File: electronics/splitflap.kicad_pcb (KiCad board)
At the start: 2 copper layers, 96 x 48 mm, 39 parts, among them CON1 MOTOR_PWR, J1 EXP. IN, J2 EXP. OUT, P1 CONN_01X05, P10 CONN_01X04, P2 CONN_01X05, P3 CONN_01X05, P4 CONN_01X05, P6 CONN_01X04, P7 CONN_01X04, P8 CONN_01X04, U1 arduino_uno_shield, U2 MIC5842, U3 74HC165, U4 MIC5842, U5 WS2812B, U6 WS2812B, U7 WS2812B, U8 WS2812B

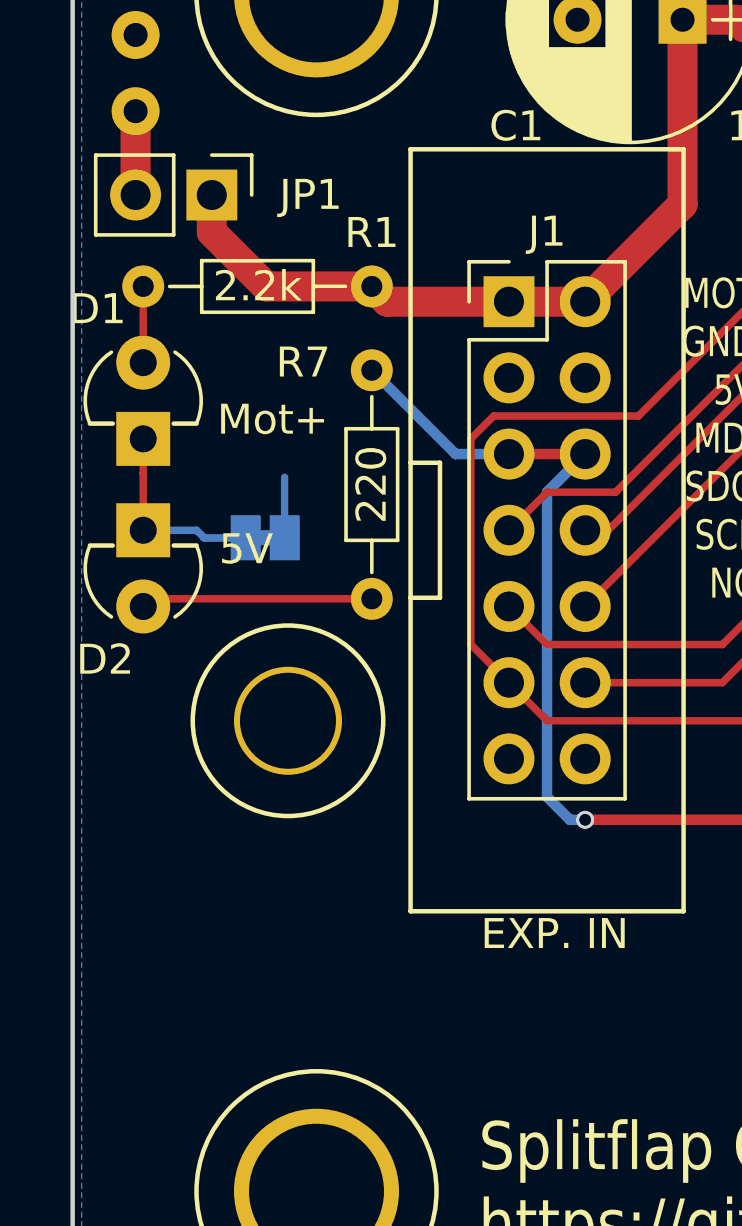
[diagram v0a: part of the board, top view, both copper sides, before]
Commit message: Move power LEDs lower
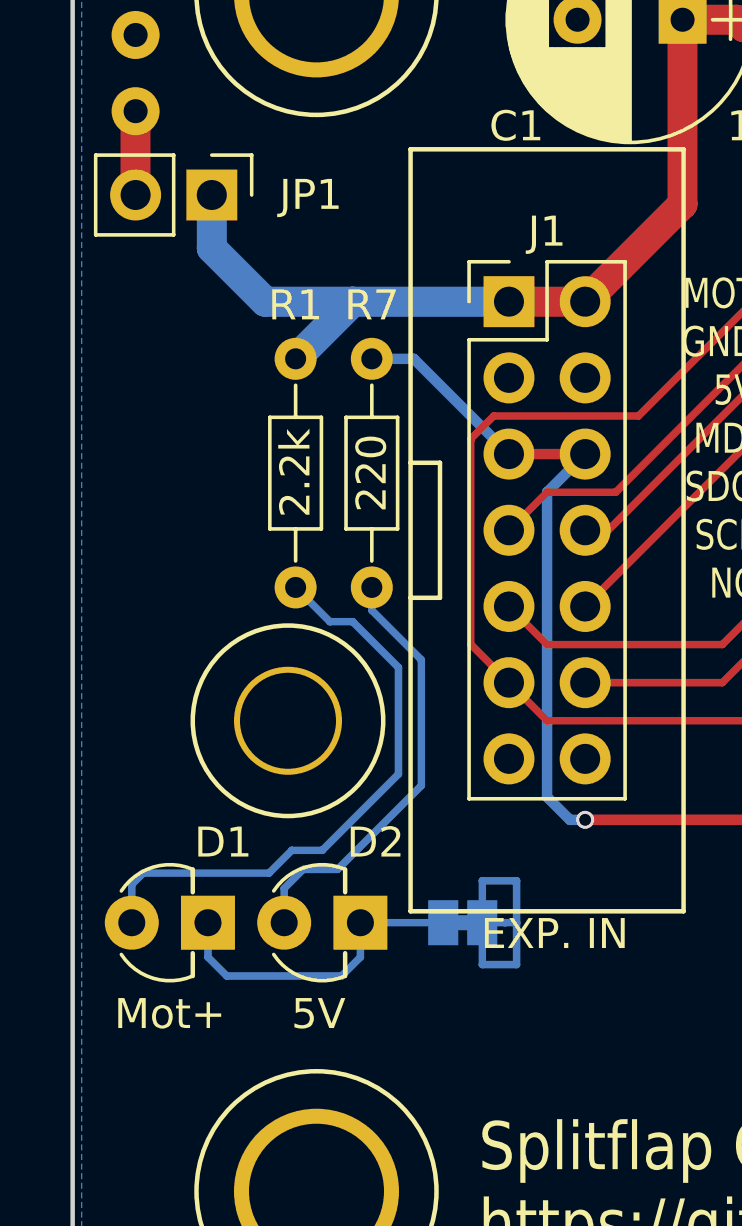
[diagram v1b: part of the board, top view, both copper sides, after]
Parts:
- moved D1 16.3 mm to (24.5, 55.0), turned to 180 degrees
- moved D2 15.0 mm to (29.6, 55.0), turned to 180 degrees
- moved JP2 14.4 mm to (33.0, 55.0)
- moved R1 11.2 mm to (27.4, 43.8), turned to 90 degrees
- moved R7 0.38 mm to (30.0, 43.8)
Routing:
- net Net-(D1-Pad2): track 2.54 -> 19.8 mm
- net GND: track 7.76 -> 14.8 mm
- net Net-(D2-Pad2): track 7.73 -> 14.4 mm
- net Net-(D1-Pad1): track 6.57 -> 10.7 mm
- net VCC: track 126.4 -> 129.4 mm
